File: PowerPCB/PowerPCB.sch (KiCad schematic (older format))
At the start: 1 part

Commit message: Added inital components
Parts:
- added C? (x2): C, symbol Device:C
- added D?: DIODE, symbol pspice:DIODE
- added D? (x3): LED, symbol Device:LED
- added J?: Conn_01x03_Male, symbol Connector:Conn_01x03_Male
- added J?: STM Inputs, symbol Connector:Conn_01x07_Male
- added J?: Conn_01x07_Male, symbol Connector:Conn_01x07_Male
- added J?: STM Outputs, symbol Connector:Conn_01x07_Male
- added K?: HF3-06, Relay_SMD:Relay_SPDT_AXICOM_HF3Series_75ohms_Pitch1.27mm, symbol Relay:HF3-06
- added R? (x4): R, symbol Device:R
- added U?: NCP1117-3.3_SOT223, Package_TO_SOT_SMD:SOT-223-3_TabPin2, symbol Regulator_Linear:NCP1117-3.3_SOT223
- J?: value Conn_01x05_Male -> Conn_01x08_Male; symbol Connector:Conn_01x05_Male -> Connector:Conn_01x08_Male
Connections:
- net labels added: GND
- wire segments 0 -> 69
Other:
- note added: "12 V +\n12 V -\n"
- note added: "AUX +\nAUX -\nDCDC +\nDCDC -\nFAN\nCHARGE\nREADY"
- note added: "CAN HI\nCAN LO\nCAN GND"
- note added: "CAN HI\nCAN LO\nCAN GND\nAUX +\nDCDC +\nPOWER +\nPOWER -"
- note removed: "A\nB\nC\nD\nE"

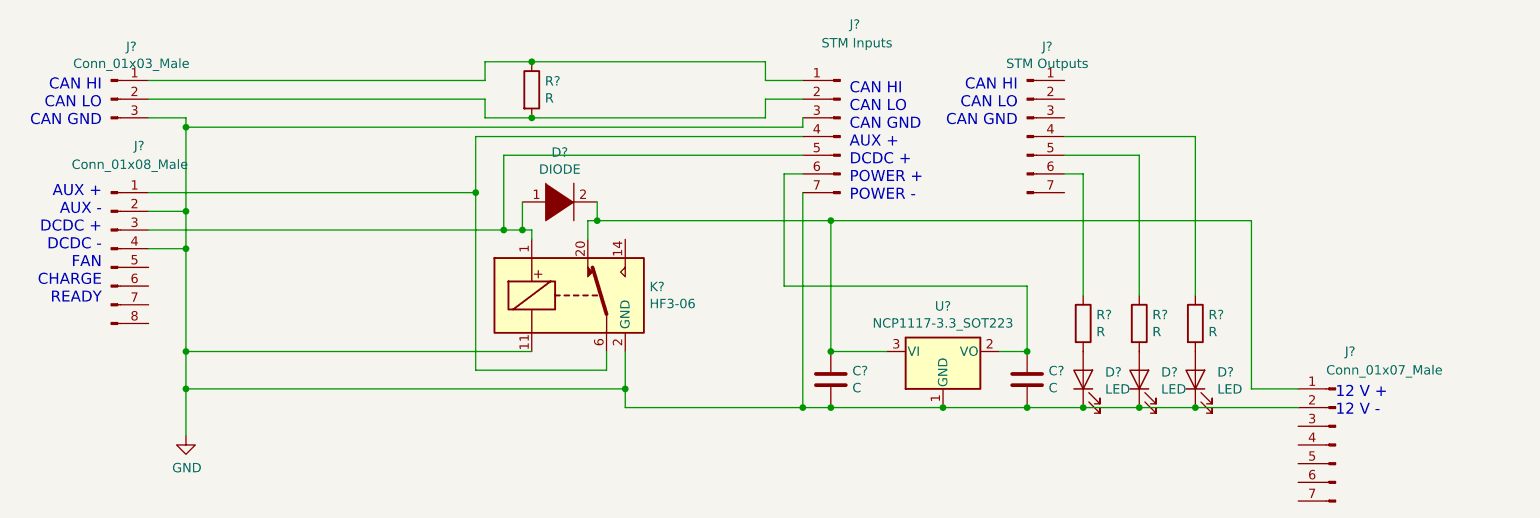
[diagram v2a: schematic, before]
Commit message: Added Voltage Divider to PowerPCB for stepping down AUX voltage before outputting it to STM
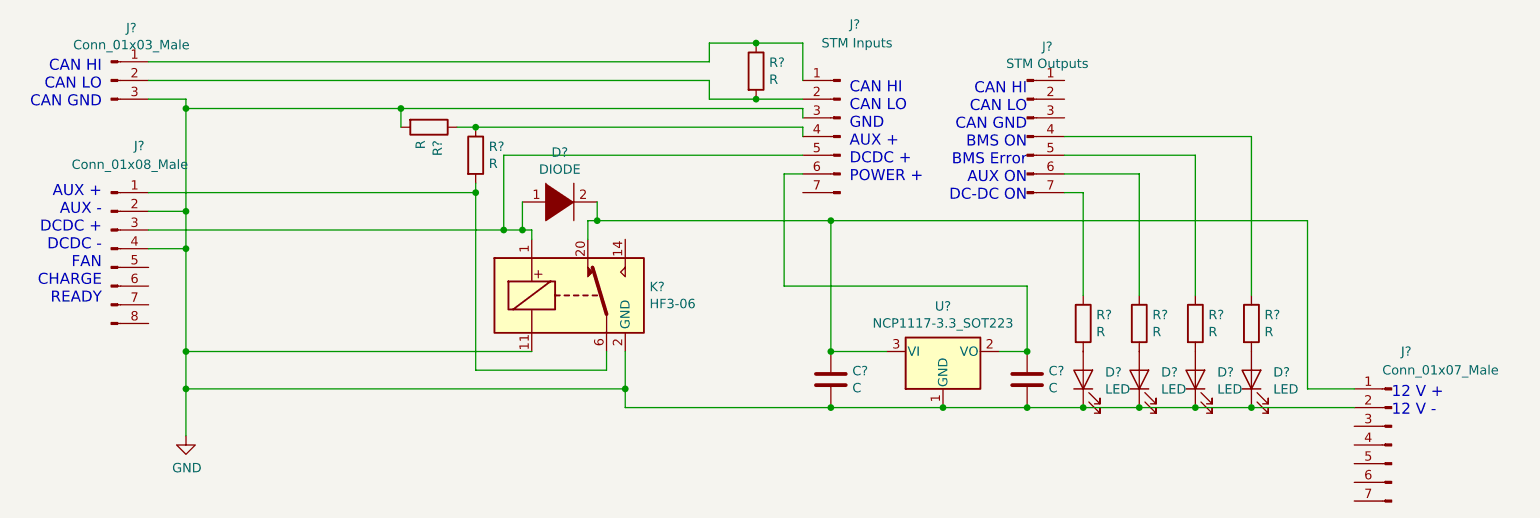
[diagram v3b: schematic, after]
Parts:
- added D?: LED, symbol Device:LED
- added R? (x3): R, symbol Device:R
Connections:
- net GND: now also D?.1 (K), R?.2; no longer J?.7 (Pin_7)
- net at J?.1 (Pin_1), K?.6: now also R?.2; no longer J?.4 (Pin_4)
- net at J?.7 (Pin_7): now also R?.1
- new net: J?.4 (Pin_4), R?.1, R?.1
- new net: D?.2 (A), R?.2
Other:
- note added: "CAN HI\nCAN LO\nCAN GND\nBMS ON\nBMS Error\nAUX ON\nDC-DC ON"
- note added: "CAN HI\nCAN LO\nGND\nAUX +\nDCDC +\nPOWER +"
- note removed: "CAN HI\nCAN LO\nCAN GND\nAUX +\nDCDC +\nPOWER +\nPOWER -"
- moved on the sheet: D?, J?, R?

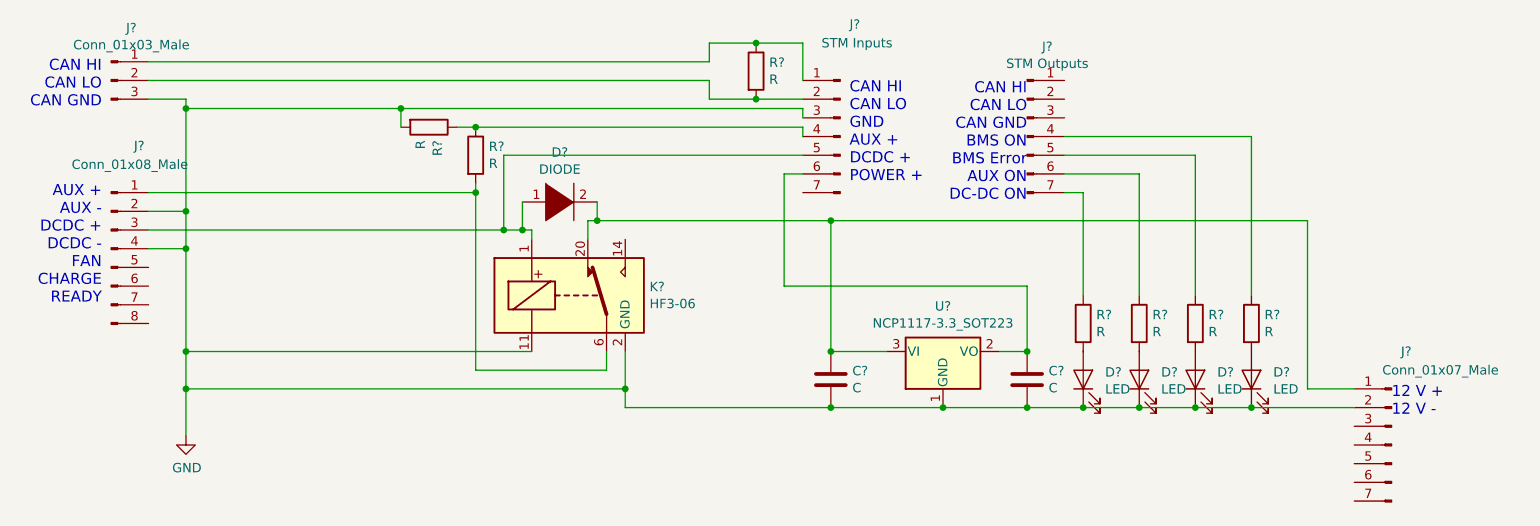
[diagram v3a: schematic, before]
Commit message: Added Fan circuit as hierarchical block to main PCB
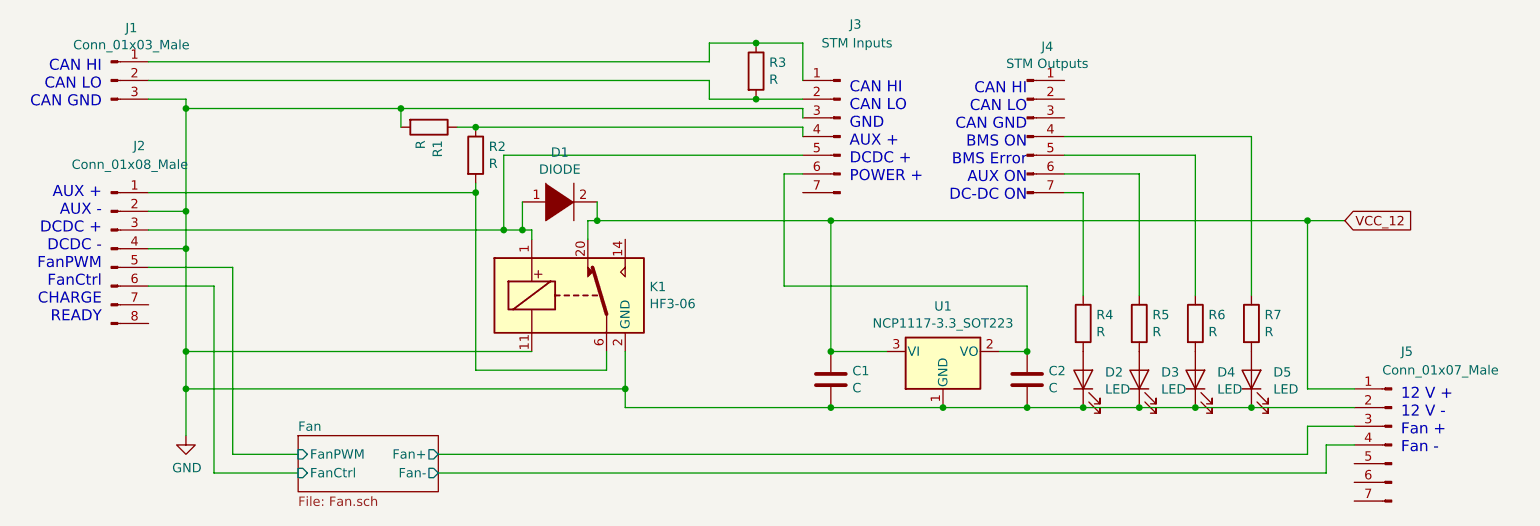
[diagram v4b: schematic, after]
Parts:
- gave numbers to parts that had none: 21
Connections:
- net Fan/FanPWM: now reaches J2.5 (Pin_5)
- net Fan/FanCtrl: now reaches J2.6 (Pin_6)
- net VCC_12: now reaches C1.1, D1.2 (A), J5.1 (Pin_1), K1.20, U1.3 (VI)
- net Fan/Fan+: now reaches J5.3 (Pin_3)
- net Fan/Fan-: now reaches J5.4 (Pin_4)
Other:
- note added: "12 V +\n12 V -\nFan +\nFan -"
- note added: "AUX +\nAUX -\nDCDC +\nDCDC -\nFanPWM\nFanCtrl\nCHARGE\nREADY"
- note removed: "12 V +\n12 V -\n"
- note removed: "AUX +\nAUX -\nDCDC +\nDCDC -\nFAN\nCHARGE\nREADY"
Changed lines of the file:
@@
 $Descr A4 11693 8268
 encoding utf-8
-Sheet 1 1
+Sheet 1 2
 Title ""
 Date ""
@@
 $EndDescr
 $Comp
-L Device:R R?
+L Device:R R3
 U 1 1 5E949A12
 P 4750 1500
-F 0 "R?" H 4820 1546 50  0000 L CNN
+F 0 "R3" H 4820 1546 50  0000 L CNN
 F 1 "R" H 4820 1455 50  0000 L CNN
 F 2 "" V 4680 1500 50  0001 C CNN
@@
 	1500 1650 1700 1650
 $Comp
-L Relay:HF3-06 K?
+L Relay:HF3-06 K1
 U 1 1 5E94CB7B
 P 3750 2700
-F 0 "K?" H 4180 2746 50  0000 L CNN
+F 0 "K1" H 4180 2746 50  0000 L CNN
 F 1 "HF3-06" H 4180 2655 50  0000 L CNN
 F 2 "Relay_SMD:Relay_SPDT_AXICOM_HF3Series_75ohms_Pitch1.27mm" H 4880 2670 50  0001 C CNN
@@
 Connection ~ 5150 3000
 $Comp
-L Device:C C?
+L Device:C C1
 U 1 1 5E9AFBC4
 P 5150 3150
-F 0 "C?" H 5265 3196 50  0000 L CNN
+F 0 "C1" H 5265 3196 50  0000 L CNN
 F 1 "C" H 5265 3105 50  0000 L CNN
 F 2 "" H 5188 3000 50  0001 C CNN
@@
 Connection ~ 6200 3000
 $Comp
-L Device:C C?
+L Device:C C2
 U 1 1 5E9AEA5E
 P 6200 3150
-F 0 "C?" H 6315 3196 50  0000 L CNN
+F 0 "C2" H 6315 3196 50  0000 L CNN
 F 1 "C" H 6315 3105 50  0000 L CNN
 F 2 "" H 6238 3000 50  0001 C CNN
@@
 Connection ~ 5750 3300
 $Comp
-L Regulator_Linear:NCP1117-3.3_SOT223 U?
+L Regulator_Linear:NCP1117-3.3_SOT223 U1
 U 1 1 5E9953A6
 P 5750 3000
-F 0 "U?" H 5750 3242 50  0000 C CNN
+F 0 "U1" H 5750 3242 50  0000 C CNN
 F 1 "NCP1117-3.3_SOT223" H 5750 3151 50  0000 C CNN
 F 2 "Package_TO_SOT_SMD:SOT-223-3_TabPin2" H 5750 3200 50  0001 C CNN
@@
 Connection ~ 6800 3300
 $Comp
-L Device:R R?
+L Device:R R5
 U 1 1 5E984DE8
 P 6800 2850
-F 0 "R?" H 6870 2896 50  0000 L CNN
+F 0 "R5" H 6870 2896 50  0000 L CNN
 F 1 "R" H 6870 2805 50  0000 L CNN
 F 2 "" V 6730 2850 50  0001 C CNN
@@
 $EndComp
 $Comp
-L Device:LED D?
+L Device:LED D3
 U 1 1 5E984DE2
 P 6800 3150
-F 0 "D?" V 6839 3033 50  0000 R CNN
+F 0 "D3" V 6839 3033 50  0000 R CNN
 F 1 "LED" V 6748 3033 50  0000 R CNN
 F 2 "" H 6800 3150 50  0001 C CNN
@@
 $EndComp
 $Comp
-L Device:R R?
+L Device:R R6
 U 1 1 5E980DA5
 P 7100 2850
-F 0 "R?" H 7170 2896 50  0000 L CNN
+F 0 "R6" H 7170 2896 50  0000 L CNN
 F 1 "R" H 7170 2805 50  0000 L CNN
 F 2 "" V 7030 2850 50  0001 C CNN
@@
 $EndComp
 $Comp
-L Device:LED D?
+L Device:LED D4
 U 1 1 5E980D9F
 P 7100 3150
-F 0 "D?" V 7139 3033 50  0000 R CNN
+F 0 "D4" V 7139 3033 50  0000 R CNN
 F 1 "LED" V 7048 3033 50  0000 R CNN
 F 2 "" H 7100 3150 50  0001 C CNN
@@
 	7400 2700 7400 1850
 $Comp
-L Device:R R?
+L Device:R R7
 U 1 1 5E97E448
 P 7400 2850
-F 0 "R?" H 7470 2896 50  0000 L CNN
+F 0 "R7" H 7470 2896 50  0000 L CNN
 F 1 "R" H 7470 2805 50  0000 L CNN
 F 2 "" V 7330 2850 50  0001 C CNN
@@
 Connection ~ 7400 3300
 $Comp
-L Device:LED D?
+L Device:LED D5
 U 1 1 5E979B1E
 P 7400 3150
-F 0 "D?" V 7439 3033 50  0000 R CNN
+F 0 "D5" V 7439 3033 50  0000 R CNN
 F 1 "LED" V 7348 3033 50  0000 R CNN
 F 2 "" H 7400 3150 50  0001 C CNN
@@
 $EndComp
 $Comp
-L Connector:Conn_01x07_Male J?
+L Connector:Conn_01x07_Male J4
 U 1 1 5E97258B
 P 6200 1850
-F 0 "J?" H 6308 2331 50  0000 C CNN
+F 0 "J4" H 6308 2331 50  0000 C CNN
 F 1 "STM Outputs" H 6308 2240 50  0000 C CNN
 F 2 "" H 6200 1850 50  0001 C CNN
@@
 	1500 2350 3400 2350
 $Comp
-L pspice:DIODE D?
+L pspice:DIODE D1
 U 1 1 5E95329D
 P 3700 2200
-F 0 "D?" H 3700 2465 50  0000 C CNN
+F 0 "D1" H 3700 2465 50  0000 C CNN
 F 1 "DIODE" H 3700 2374 50  0000 C CNN
 F 2 "" H 3700 2200 50  0001 C CNN
@@
 	1    0    0    -1
 $EndComp
-Text Notes 8150 3350 0    59   ~ 0
-12 V +\n12 V -\n
-$Comp
-L Connector:Conn_01x07_Male J?
+Text Notes 8200 3550 0    59   ~ 0
+12 V +\n12 V -\nFan +\nFan -
+$Comp
+L Connector:Conn_01x07_Male J5
 U 1 1 5E941799
 P 8150 3500
-F 0 "J?" H 8100 4000 50  0000 R CNN
+F 0 "J5" H 8100 4000 50  0000 R CNN
 F 1 "Conn_01x07_Male" H 8200 3900 50  0000 R CNN
 F 2 "" H 8150 3500 50  0001 C CNN
@@
 CAN HI\nCAN LO\nGND\nAUX +\nDCDC +\nPOWER +
 $Comp
-L Connector:Conn_01x07_Male J?
+L Connector:Conn_01x07_Male J3
 U 1 1 5E93AAC1
 P 5200 1850
-F 0 "J?" H 5150 2450 50  0000 R CNN
+F 0 "J3" H 5150 2450 50  0000 R CNN
 F 1 "STM Inputs" H 5300 2350 50  0000 R CNN
 F 2 "" H 5200 1850 50  0001 C CNN
@@
 $EndComp
 $Comp
-L Connector:Conn_01x08_Male J?
+L Connector:Conn_01x08_Male J2
 U 1 1 5E89F68E
 P 1300 2450
-F 0 "J?" H 1450 3000 50  0000 C CNN
+F 0 "J2" H 1450 3000 50  0000 C CNN
 F 1 "Conn_01x08_Male" H 1400 2900 50  0000 C CNN
 F 2 "" H 1300 2450 50  0001 C CNN
@@
 CAN HI\nCAN LO\nCAN GND
 $Comp
-L Connector:Conn_01x03_Male J?
+L Connector:Conn_01x03_Male J1
 U 1 1 5E933C76
 P 1300 1550
-F 0 "J?" H 1408 1831 50  0000 C CNN
+F 0 "J1" H 1408 1831 50  0000 C CNN
 F 1 "Conn_01x03_Male" H 1408 1740 50  0000 C CNN
 F 2 "" H 1300 1550 50  0001 C CNN
@@
 	1    0    0    -1
 $EndComp
-Text Notes 1250 2750 2    59   ~ 0
-AUX +\nAUX -\nDCDC +\nDCDC -\nFAN\nCHARGE\nREADY
+Text Notes 1250 2850 2    59   ~ 0
+AUX +\nAUX -\nDCDC +\nDCDC -\nFanPWM\nFanCtrl\nCHARGE\nREADY
 Wire Wire Line
 	1500 2150 3250 2150
@@
 	5000 1800 5000 1850
 $Comp
-L Device:R R?
+L Device:R R2
 U 1 1 5EAB437C
 P 3250 1950
-F 0 "R?" H 3320 1996 50  0000 L CNN
+F 0 "R2" H 3320 1996 50  0000 L CNN
 F 1 "R" H 3320 1905 50  0000 L CNN
 F 2 "" V 3180 1950 50  0001 C CNN
@@
 	3250 2100 3250 2150
 $Comp
-L Device:R R?
+L Device:R R1
 U 1 1 5EAB4924
 P 3000 1800
-F 0 "R?" H 3070 1846 50  0000 L CNN
+F 0 "R1" H 3070 1846 50  0000 L CNN
 F 1 "R" H 3070 1755 50  0000 L CNN
 F 2 "" V 2930 1800 50  0001 C CNN
@@
 	6400 1850 7400 1850
 $Comp
-L Device:R R?
+L Device:R R4
 U 1 1 5EADC389
 P 6500 2850
-F 0 "R?" H 6570 2896 50  0000 L CNN
+F 0 "R4" H 6570 2896 50  0000 L CNN
 F 1 "R" H 6570 2805 50  0000 L CNN
 F 2 "" V 6430 2850 50  0001 C CNN
@@
 $EndComp
 $Comp
-L Device:LED D?
+L Device:LED D2
 U 1 1 5EADC907
 P 6500 3150
-F 0 "D?" V 6539 3033 50  0000 R CNN
+F 0 "D2" V 6539 3033 50  0000 R CNN
 F 1 "LED" V 6448 3033 50  0000 R CNN
 F 2 "" H 6500 3150 50  0001 C CNN
@@
 Wire Wire Line
 	6500 2150 6400 2150
+$Sheet
+S 2300 3450 750  300
+U 5EC1CC82
+F0 "Fan" 50
+F1 "Fan.sch" 50
+F2 "FanPWM" I L 2300 3550 50
+F3 "Fan+" O R 3050 3550 50
+F4 "Fan-" O R 3050 3650 50
+F5 "FanCtrl" I L 2300 3650 50
+$EndSheet
+Text GLabel 7900 2300 2    50   Input ~ 0
+VCC_12
+Wire Wire Line
+	7900 2300 7700 2300
+Connection ~ 7700 2300
+Wire Wire Line
+	1500 2550 1950 2550
+Wire Wire Line
+	1950 2550 1950 3550
+Wire Wire Line
+	1950 3550 2300 3550
+Wire Wire Line
+	1500 2650 1850 2650
+Wire Wire Line
+	1850 2650 1850 3650
+Wire Wire Line
+	1850 3650 2300 3650
+Wire Wire Line
+	3050 3550 7700 3550
+Wire Wire Line
+	7700 3550 7700 3400
+Wire Wire Line
+	7700 3400 7950 3400
+Wire Wire Line
+	3050 3650 7800 3650
+Wire Wire Line
+	7800 3650 7800 3500
+Wire Wire Line
+	7800 3500 7950 3500
 $EndSCHEMATC

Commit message: Added footprints for all components
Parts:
- C1, C2: footprint (none) -> Capacitor_SMD:C_0805_2012Metric_Pad1.15x1.40mm_HandSolder
- D1: footprint (none) -> Diode_SMD:D_0805_2012Metric_Pad1.15x1.40mm_HandSolder
- D2, D3, D4, D5: footprint (none) -> LED_SMD:LED_0805_2012Metric_Pad1.15x1.40mm_HandSolder
- J1: footprint (none) -> Connector_PinHeader_1.00mm:PinHeader_1x03_P1.00mm_Vertical
- J2: footprint (none) -> Connector_PinHeader_1.00mm:PinHeader_1x08_P1.00mm_Vertical
- J3, J4, J5: footprint (none) -> Connector_PinHeader_1.00mm:PinHeader_1x07_P1.00mm_Vertical
- R1, R2, R3, R4, R5, R6, R7: footprint (none) -> Resistor_SMD:R_0805_2012Metric_Pad1.15x1.40mm_HandSolder
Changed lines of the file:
@@
 F 0 "R3" H 4820 1546 50  0000 L CNN
 F 1 "R" H 4820 1455 50  0000 L CNN
-F 2 "" V 4680 1500 50  0001 C CNN
+F 2 "Resistor_SMD:R_0805_2012Metric_Pad1.15x1.40mm_HandSolder" V 4680 1500 50  0001 C CNN
 F 3 "~" H 4750 1500 50  0001 C CNN
 	1    4750 1500
@@
 F 0 "C1" H 5265 3196 50  0000 L CNN
 F 1 "C" H 5265 3105 50  0000 L CNN
-F 2 "" H 5188 3000 50  0001 C CNN
+F 2 "Capacitor_SMD:C_0805_2012Metric_Pad1.15x1.40mm_HandSolder" H 5188 3000 50  0001 C CNN
 F 3 "~" H 5150 3150 50  0001 C CNN
 	1    5150 3150
@@
 F 0 "C2" H 6315 3196 50  0000 L CNN
 F 1 "C" H 6315 3105 50  0000 L CNN
-F 2 "" H 6238 3000 50  0001 C CNN
+F 2 "Capacitor_SMD:C_0805_2012Metric_Pad1.15x1.40mm_HandSolder" H 6238 3000 50  0001 C CNN
 F 3 "~" H 6200 3150 50  0001 C CNN
 	1    6200 3150
@@
 F 0 "R5" H 6870 2896 50  0000 L CNN
 F 1 "R" H 6870 2805 50  0000 L CNN
-F 2 "" V 6730 2850 50  0001 C CNN
+F 2 "Resistor_SMD:R_0805_2012Metric_Pad1.15x1.40mm_HandSolder" V 6730 2850 50  0001 C CNN
 F 3 "~" H 6800 2850 50  0001 C CNN
 	1    6800 2850
@@
 F 0 "D3" V 6839 3033 50  0000 R CNN
 F 1 "LED" V 6748 3033 50  0000 R CNN
-F 2 "" H 6800 3150 50  0001 C CNN
+F 2 "LED_SMD:LED_0805_2012Metric_Pad1.15x1.40mm_HandSolder" H 6800 3150 50  0001 C CNN
 F 3 "~" H 6800 3150 50  0001 C CNN
 	1    6800 3150
@@
 F 0 "R6" H 7170 2896 50  0000 L CNN
 F 1 "R" H 7170 2805 50  0000 L CNN
-F 2 "" V 7030 2850 50  0001 C CNN
+F 2 "Resistor_SMD:R_0805_2012Metric_Pad1.15x1.40mm_HandSolder" V 7030 2850 50  0001 C CNN
 F 3 "~" H 7100 2850 50  0001 C CNN
 	1    7100 2850
@@
 F 0 "D4" V 7139 3033 50  0000 R CNN
 F 1 "LED" V 7048 3033 50  0000 R CNN
-F 2 "" H 7100 3150 50  0001 C CNN
+F 2 "LED_SMD:LED_0805_2012Metric_Pad1.15x1.40mm_HandSolder" H 7100 3150 50  0001 C CNN
 F 3 "~" H 7100 3150 50  0001 C CNN
 	1    7100 3150
@@
 F 0 "R7" H 7470 2896 50  0000 L CNN
 F 1 "R" H 7470 2805 50  0000 L CNN
-F 2 "" V 7330 2850 50  0001 C CNN
+F 2 "Resistor_SMD:R_0805_2012Metric_Pad1.15x1.40mm_HandSolder" V 7330 2850 50  0001 C CNN
 F 3 "~" H 7400 2850 50  0001 C CNN
 	1    7400 2850
@@
 F 0 "D5" V 7439 3033 50  0000 R CNN
 F 1 "LED" V 7348 3033 50  0000 R CNN
-F 2 "" H 7400 3150 50  0001 C CNN
+F 2 "LED_SMD:LED_0805_2012Metric_Pad1.15x1.40mm_HandSolder" H 7400 3150 50  0001 C CNN
 F 3 "~" H 7400 3150 50  0001 C CNN
 	1    7400 3150
@@
 F 0 "J4" H 6308 2331 50  0000 C CNN
 F 1 "STM Outputs" H 6308 2240 50  0000 C CNN
-F 2 "" H 6200 1850 50  0001 C CNN
+F 2 "Connector_PinHeader_1.00mm:PinHeader_1x07_P1.00mm_Vertical" H 6200 1850 50  0001 C CNN
 F 3 "~" H 6200 1850 50  0001 C CNN
 	1    6200 1850
@@
 F 0 "D1" H 3700 2465 50  0000 C CNN
 F 1 "DIODE" H 3700 2374 50  0000 C CNN
-F 2 "" H 3700 2200 50  0001 C CNN
+F 2 "Diode_SMD:D_0805_2012Metric_Pad1.15x1.40mm_HandSolder" H 3700 2200 50  0001 C CNN
 F 3 "~" H 3700 2200 50  0001 C CNN
 	1    3700 2200
@@
 F 0 "J5" H 8100 4000 50  0000 R CNN
 F 1 "Conn_01x07_Male" H 8200 3900 50  0000 R CNN
-F 2 "" H 8150 3500 50  0001 C CNN
+F 2 "Connector_PinHeader_1.00mm:PinHeader_1x07_P1.00mm_Vertical" H 8150 3500 50  0001 C CNN
 F 3 "~" H 8150 3500 50  0001 C CNN
 	1    8150 3500
@@
 F 0 "J3" H 5150 2450 50  0000 R CNN
 F 1 "STM Inputs" H 5300 2350 50  0000 R CNN
-F 2 "" H 5200 1850 50  0001 C CNN
+F 2 "Connector_PinHeader_1.00mm:PinHeader_1x07_P1.00mm_Vertical" H 5200 1850 50  0001 C CNN
 F 3 "~" H 5200 1850 50  0001 C CNN
 	1    5200 1850
@@
 F 0 "J2" H 1450 3000 50  0000 C CNN
 F 1 "Conn_01x08_Male" H 1400 2900 50  0000 C CNN
-F 2 "" H 1300 2450 50  0001 C CNN
+F 2 "Connector_PinHeader_1.00mm:PinHeader_1x08_P1.00mm_Vertical" H 1300 2450 50  0001 C CNN
 F 3 "~" H 1300 2450 50  0001 C CNN
 	1    1300 2450
@@
 F 0 "J1" H 1408 1831 50  0000 C CNN
 F 1 "Conn_01x03_Male" H 1408 1740 50  0000 C CNN
-F 2 "" H 1300 1550 50  0001 C CNN
+F 2 "Connector_PinHeader_1.00mm:PinHeader_1x03_P1.00mm_Vertical" H 1300 1550 50  0001 C CNN
 F 3 "~" H 1300 1550 50  0001 C CNN
 	1    1300 1550
@@
 F 0 "R2" H 3320 1996 50  0000 L CNN
 F 1 "R" H 3320 1905 50  0000 L CNN
-F 2 "" V 3180 1950 50  0001 C CNN
+F 2 "Resistor_SMD:R_0805_2012Metric_Pad1.15x1.40mm_HandSolder" V 3180 1950 50  0001 C CNN
 F 3 "~" H 3250 1950 50  0001 C CNN
 	1    3250 1950
@@
 F 0 "R1" H 3070 1846 50  0000 L CNN
 F 1 "R" H 3070 1755 50  0000 L CNN
-F 2 "" V 2930 1800 50  0001 C CNN
+F 2 "Resistor_SMD:R_0805_2012Metric_Pad1.15x1.40mm_HandSolder" V 2930 1800 50  0001 C CNN
 F 3 "~" H 3000 1800 50  0001 C CNN
 	1    3000 1800
@@
 F 0 "R4" H 6570 2896 50  0000 L CNN
 F 1 "R" H 6570 2805 50  0000 L CNN
-F 2 "" V 6430 2850 50  0001 C CNN
+F 2 "Resistor_SMD:R_0805_2012Metric_Pad1.15x1.40mm_HandSolder" V 6430 2850 50  0001 C CNN
 F 3 "~" H 6500 2850 50  0001 C CNN
 	1    6500 2850
@@
 F 0 "D2" V 6539 3033 50  0000 R CNN
 F 1 "LED" V 6448 3033 50  0000 R CNN
-F 2 "" H 6500 3150 50  0001 C CNN
+F 2 "LED_SMD:LED_0805_2012Metric_Pad1.15x1.40mm_HandSolder" H 6500 3150 50  0001 C CNN
 F 3 "~" H 6500 3150 50  0001 C CNN
 	1    6500 3150

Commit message: Imported components to PCBnew
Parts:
- added U2: STM32F413ZHTx, Package_QFP:LQFP-144_20x20mm_P0.5mm, symbol MCU_ST_STM32F4:STM32F413ZHTx
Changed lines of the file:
@@
 Wire Wire Line
 	7800 3500 7950 3500
+$Comp
+L MCU_ST_STM32F4:STM32F413ZHTx U2
+U 1 1 5ECD68BB
+P 10200 4100
+F 0 "U2" H 10200 411 50  0000 C CNN
+F 1 "STM32F413ZHTx" H 10200 320 50  0000 C CNN
+F 2 "Package_QFP:LQFP-144_20x20mm_P0.5mm" H 9200 700 50  0001 R CNN
+F 3 "http://www.st.com/st-web-ui/static/active/en/resource/technical/document/datasheet/DM00282249.pdf" H 10200 4100 50  0001 C CNN
+	1    10200 4100
+	1    0    0    -1
+$EndComp
 $EndSCHEMATC
